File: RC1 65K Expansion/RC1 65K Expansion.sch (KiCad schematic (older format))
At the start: 13 parts, among them J1 Expansion, U1 74LS138, U2 74LS145, U3 74LS08

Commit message: 65K layout and silkscreen done
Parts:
- added C4: 100nF, Capacitors_THT:C_Disc_D4.7mm_W2.5mm_P5.00mm, symbol C
- added J2: External IO, Pin_Headers:Pin_Header_Straight_2x10_Pitch2.54mm, symbol Conn_02x10_Odd_Even
- added J3: Extra, Pin_Headers:Pin_Header_Straight_1x03_Pitch2.54mm, symbol Conn_01x03
- added JP5: IRQ_EN, Pin_Headers:Pin_Header_Straight_1x03_Pitch2.54mm, symbol Jumper_NC_Dual
- added JP6: 6532_EN, Pin_Headers:Pin_Header_Straight_1x03_Pitch2.54mm, symbol Jumper_NC_Dual
- added JP7: 8K7_ROM, Pin_Headers:Pin_Header_Straight_1x03_Pitch2.54mm, symbol Jumper_NC_Dual
- added U4: R6532, Housings_DIP:DIP-40_W15.24mm_Socket, symbol R6532
- JP1, JP2, JP3, JP4: footprint (none) -> Pin_Headers:Pin_Header_Straight_1x03_Pitch2.54mm
- U3: footprint (none) -> Housings_DIP:DIP-14_W7.62mm_Socket
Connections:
- net 8K1: now also JP1.1; no longer JP1.3
- net 8K2: now also JP2.1; no longer JP2.3
- net 8K3: now also JP4.1; no longer JP4.3
- net 8K7: now also JP7.1; no longer U3.4
- net GND: now also C4.2, J2.1 (Pin_1), J2.19 (Pin_19), J2.2 (Pin_2), U4.1 (GND)
- net ORG_RAM: now also R1.1; no longer R1.2
- net ORG_ROM: now also JP3.1; no longer JP3.3
- net VCC: now also JP1.3, JP2.3, JP3.3, JP4.3, R1.2, C4.1, J2.20 (Pin_20), JP5.3, JP6.3, JP7.3, U4.20 (VCC), U4.36 (~RS), U4.38 (CS1); no longer JP1.1, JP2.1, JP3.1, JP4.1, R1.1
- net A6: now reaches J1.10 (A6)
- net A6: now also U4.40 (A6)
- net A5: now reaches J1.11 (A5)
- net A5: now also U4.2 (A5)
- net A4: now reaches J1.12 (A4)
- net A4: now also U4.3 (A4)
- net A3: now reaches J1.13 (A3)
- net A3: now also U4.4 (A3)
- net A2: now reaches J1.14 (A2)
- net A2: now also U4.5 (A2)
- net A1: now reaches J1.15 (A1)
- net A1: now also U4.6 (A1)
- net A0: now reaches J1.16 (A0)
- net A0: now also U4.7 (A0)
- net PHI2: now reaches J1.19 (PHI2)
- net PHI2: now also U4.39 (PHI2)
- net ~RESET: now reaches J1.20 (RESET)
- net ~RESET: now also U4.34 (~RESET)
- net ~IRQ_IN: now reaches J1.22 (IRQ)
- net ~IRQ_IN: now also JP5.1
- net R/~W: now reaches J1.24 (RW)
- net R/~W: now also U4.35 (R/~W)
- net D0: now reaches J1.27 (D0)
- net D0: now also U4.33 (D0)
- net D1: now reaches J1.28 (D1)
- net D1: now also U4.32 (D1)
- net D2: now reaches J1.29 (D2)
- net D2: now also U4.31 (D2)
- net D3: now reaches J1.30 (D3)
- net D3: now also U4.30 (D3)
- net D4: now reaches J1.31 (D4)
- net D4: now also U4.29 (D4)
- net D5: now reaches J1.32 (D5)
- net D5: now also U4.28 (D5)
- net D6: now reaches J1.33 (D6)
- net D6: now also U4.27 (D6)
- net D7: now reaches J1.34 (D7)
- net D7: now also U4.26 (D7)
- net at J1.38 (P38): now also JP6.1
- net 8K5: now reaches U1.10 (O5)
- net 8K5: now also J3.2 (Pin_2)
- net 8K4: now reaches U1.11 (O4)
- net 8K4: now also J3.1 (Pin_1)
- net 8K6: now reaches U1.9 (O6)
- net 8K6: now also J3.3 (Pin_3)
- new net: JP7.2, U3.4
- new net IO3: JP6.2, U4.37 (~CS2)
- new net PA0: J2.18 (Pin_18), U4.8 (PA0)
- new net PA1: J2.16 (Pin_16), U4.9 (PA1)
- new net PA2: J2.14 (Pin_14), U4.10 (PA2)
- new net PA3: J2.12 (Pin_12), U4.11 (PA3)
- new net PA4: J2.10 (Pin_10), U4.12 (PA4)
- new net PA5: J2.8 (Pin_8), U4.13 (PA5)
- new net PA6: J2.6 (Pin_6), U4.14 (PA6)
- new net PA7: J2.4 (Pin_4), U4.15 (PA7)
- new net PB0: J2.17 (Pin_17), U4.24 (PB0)
- new net PB1: J2.15 (Pin_15), U4.23 (PB1)
- new net PB2: J2.13 (Pin_13), U4.22 (PB2)
- new net PB3: J2.11 (Pin_11), U4.21 (PB3)
- new net PB4: J2.9 (Pin_9), U4.19 (PB4)
- new net PB5: J2.7 (Pin_7), U4.18 (PB5)
- new net PB6: J2.5 (Pin_5), U4.17 (PB6)
- new net PB7: J2.3 (Pin_3), U4.16 (PB7)
- new net ~IRQ: JP5.2, U4.25 (~IRQ)
- no-connect marks 34 -> 11
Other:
- note added: "The original KIM-1 only decoded what in the documentation is called the first 8KB of\nmemory space, it is however repeated in all 8KB blocks on the system. If we want to use\nthe other 56K then we need to replace the adressing logic used, this module does that as\nwell as allow the user access to unused RAM/ROM already on the CPU board of the\nRC-ONE. Optional secondary 6532 connected to IO3."
- note removed: "The original KIM-1 only decoded what in the documentation is called the first 8KB of\nmemory space, it is however repeated in all 8KB blocks on the system. If we want to use\nthe other 56K then we need to replace the adressing logic used, this module does that as\nwell as allow the user access to unused RAM/ROM already on the CPU board of the\nRC-ONE."
- moved on the sheet: C1, C2, C3, J1, JP3, U3B

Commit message: Updated 65K schematic
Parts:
- removed JP7: 8K7_ROM, Pin_Headers:Pin_Header_Straight_1x03_Pitch2.54mm, symbol Jumper_NC_Dual
- removed R1, R2: 1k, Resistors_THT:R_Axial_DIN0207_L6.3mm_D2.5mm_P10.16mm_Horizontal, symbol R
- removed U2: 74LS145, Housings_DIP:DIP-16_W7.62mm_Socket, symbol 74LS145
- added C5, C6: 100nF, Capacitors_THT:C_Disc_D4.7mm_W2.5mm_P5.00mm, symbol C
- added J4: K1-K4, Pin_Headers:Pin_Header_Straight_1x04_Pitch2.54mm, symbol Conn_01x04
- added J5: RAM_SEL, Pin_Headers:Pin_Header_Straight_2x04_Pitch2.54mm, symbol Conn_02x04_Odd_Even
- added U2: 74LS138, Housings_DIP:DIP-16_W7.62mm_Socket, symbol 74LS138
- added U5: 74LS08, Housings_DIP:DIP-14_W7.62mm_Socket, symbol 74LS08
- added U6: 74LS00, Housings_DIP:DIP-14_W7.62mm_Socket, symbol 74LS00
- JP3: value ORG_ROM -> A4_INV
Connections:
- net 8K7: now also U3.5
- net A10: now also U2.1 (A0)
- net A11: now also U2.2 (A1)
- net A12: now also U2.3 (A2)
- net A4: now also JP3.3, U6.1, U6.2; no longer U4.3 (A4)
- net DEN: now also U2.5 (E2)
- net GND: now also C5.2, C6.2, U2.4 (E1), U2.8 (GND), U5.7 (GND), U5.7 (GND), U5.7 (GND), U5.7 (GND), U6.12, U6.13, U6.7 (GND), U6.7 (GND), U6.7 (GND), U6.7 (GND)
- net VCC: now also U4.40 (A6), C5.1, C6.1, U2.16 (VCC), U2.6 (E3), U5.14 (VCC), U5.14 (VCC), U5.14 (VCC), U5.14 (VCC), U6.14 (VCC), U6.14 (VCC), U6.14 (VCC), U6.14 (VCC); no longer JP3.3
- net at U3.4: now also U5.3
- net at JP3.2: now also U4.3 (A4); no longer U3.5
- net A6: no longer names the net of J1.10 (A6)
- net A6: no longer U4.40 (A6)
- net ORG_RAM renamed ~LOW_RAM
- net ~LOW_RAM: now also J5.2 (Pin_2), J5.4 (Pin_4), J5.6 (Pin_6), J5.8 (Pin_8)
- net ORG_ROM: no longer names the net of JP3.1
- net ORG_ROM: now also U6.3
- new net: J5.3 (Pin_3), U5.6, U5.9
- new net: U5.10, U5.11
- new net: J5.5 (Pin_5), U5.8, U6.4
- new net: J5.7 (Pin_7), U6.8
- new net: U6.10, U6.6, U6.9
- new net K0: J5.1 (Pin_1), U2.15 (O0), U5.4
- new net K1: J4.1 (Pin_1), U2.14 (O1), U5.5
- new net K2: J4.2 (Pin_2), U2.13 (O2), U5.12
- new net K3: J4.3 (Pin_3), U2.12 (O3), U5.13
- new net K4: J4.4 (Pin_4), U2.11 (O4), U6.5
- new net K6: U2.9 (O6), U5.1
- new net K7: U2.7 (O7), U5.2
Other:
- note added: "1K\n2K\n4K\n5K"
- note added: "Low memory size:\n1-2\n3-4\n5-6\n7-8"
- note added: "Original 2K ROM area is mirrored\nwithin original memory map, this\nis done to ensure compatibility\nwith existing software for\nun-expanded systems."
- note added: "RAM SELECT LOGIC"
- note added: "ROM SELECT LOGIC"
- note added: "The original KIM-1 only decoded what in the documentation is called the first 8KB of\nmemory space, it is however repeated in all 8KB blocks on the system. If we want to use\nthe other 56K then we need to replace the adressing logic used, this module does that as\nwell as allow the user access to some of the unused RAM/ROM already on the CPU board\nof the RC-ONE. Optional secondary 6532 connected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"
- note added: "U4 is optional if the second 6532 for application\npurposes is not needed, U6 is also only needed\nfor 6532 or with 5K LOW RAM enabled."
- note removed: "RAM SELECT"
- note removed: "ROM SELECT"
- note removed: "The original KIM-1 only decoded what in the documentation is called the first 8KB of\nmemory space, it is however repeated in all 8KB blocks on the system. If we want to use\nthe other 56K then we need to replace the adressing logic used, this module does that as\nwell as allow the user access to unused RAM/ROM already on the CPU board of the\nRC-ONE. Optional secondary 6532 connected to IO3."
- moved on the sheet: C1, C2, C3, C4, J3, JP1, JP2, JP4, U1, U3A, U3B, U3C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

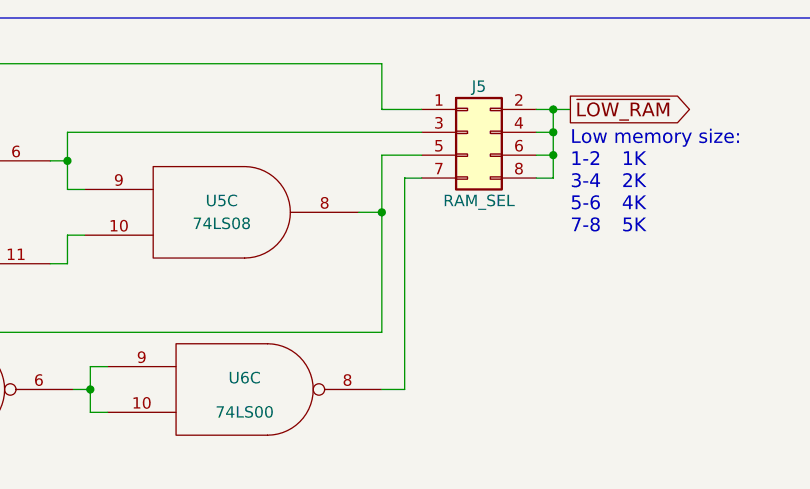
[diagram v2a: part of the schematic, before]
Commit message: 65K layout updated
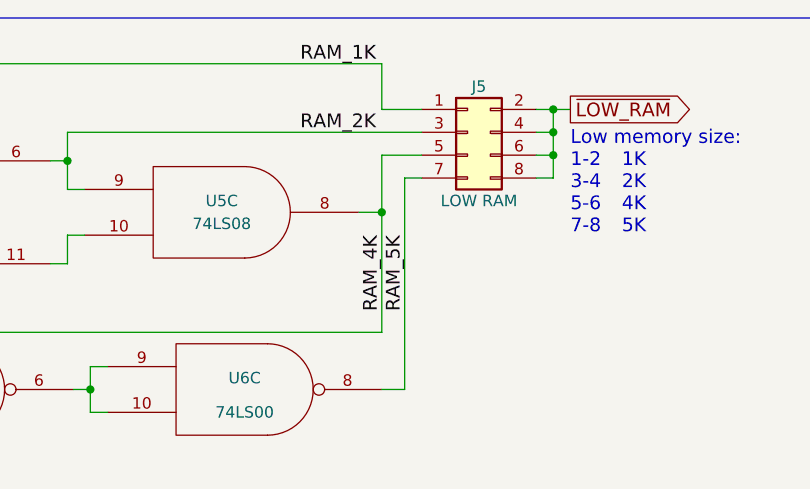
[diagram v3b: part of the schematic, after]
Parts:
- J5: value RAM_SEL -> LOW RAM
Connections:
- net RAM_2K: now reaches J5.3 (Pin_3), U5.6, U5.9
- net RAM_4K: now reaches J5.5 (Pin_5), U5.8, U6.4
- net RAM_5K: now reaches J5.7 (Pin_7), U6.8
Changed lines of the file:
@@
 P 9700 1100
 F 0 "J5" H 9750 1300 50  0000 C CNN
-F 1 "RAM_SEL" H 9750 800 50  0000 C CNN
+F 1 "LOW RAM" H 9750 800 50  0000 C CNN
 F 2 "Pin_Headers:Pin_Header_Straight_2x04_Pitch2.54mm" H 9700 1100 50  0001 C CNN
 F 3 "" H 9700 1100 50  0001 C CNN
@@
 Text Notes 1375 10000 0    60   ~ 0
 U4 is optional if the second 6532 for application\npurposes is not needed, U6 is also only needed\nfor 6532 or with 5K LOW RAM enabled.
+Text Label 9300 1100 2    60   ~ 0
+RAM_2K
+Text Label 9300 800  2    60   ~ 0
+RAM_1K
+Text Label 9325 1550 3    60   ~ 0
+RAM_4K
+Text Label 9425 1550 3    60   ~ 0
+RAM_5K
 $EndSCHEMATC

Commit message: Gerber export
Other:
- note added: "B"
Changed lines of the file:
@@
 Text Label 9425 1550 3    60   ~ 0
 RAM_5K
+Text Notes 15400 11075 0    60   ~ 0
+B
 $EndSCHEMATC
